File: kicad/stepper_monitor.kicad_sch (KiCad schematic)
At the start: 55 parts, among them J1 Conn_01x04_Male, J2 Conn_01x04_Male, J3 Conn_01x02_Male, J4 USB_C_Receptacle_USB2.0, J5 JTAG, M1 Motor-simple_stepper_motor_an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, Q1 UMH3N, Q2 PJA3439, SW1 SW_Push, U1 CP2102N-A01-GQFN28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

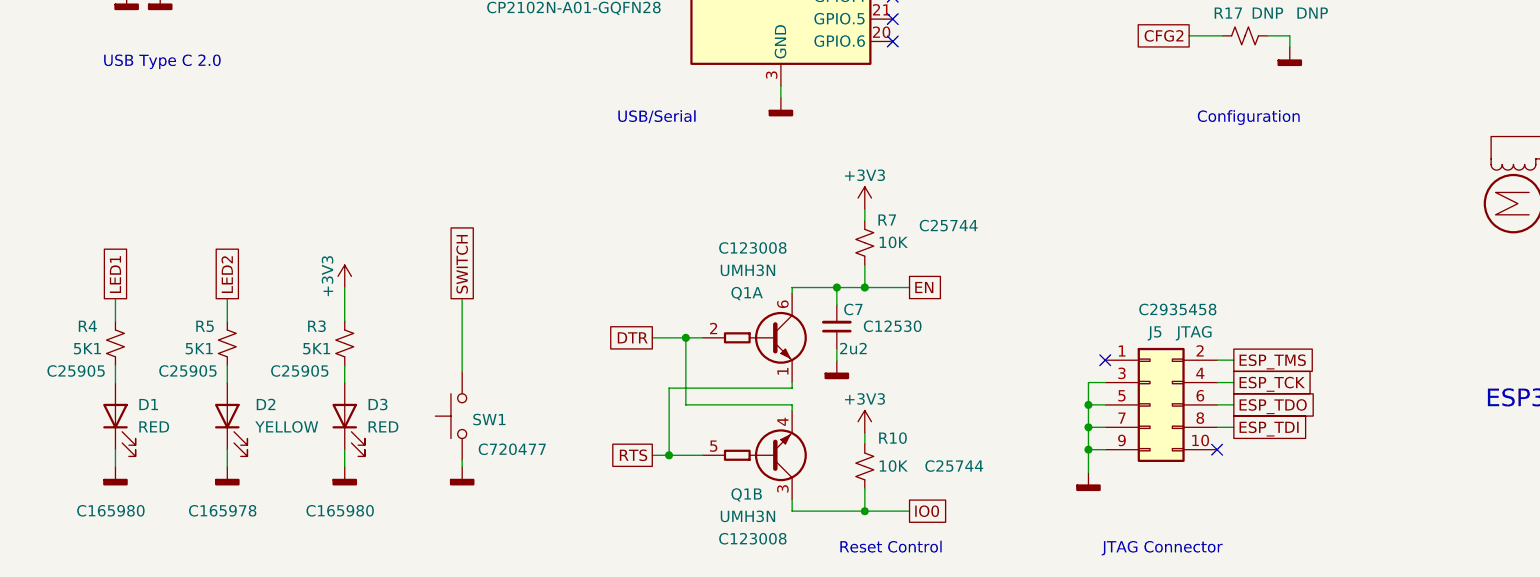
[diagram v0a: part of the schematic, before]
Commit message: Updated led and npn to available parts.
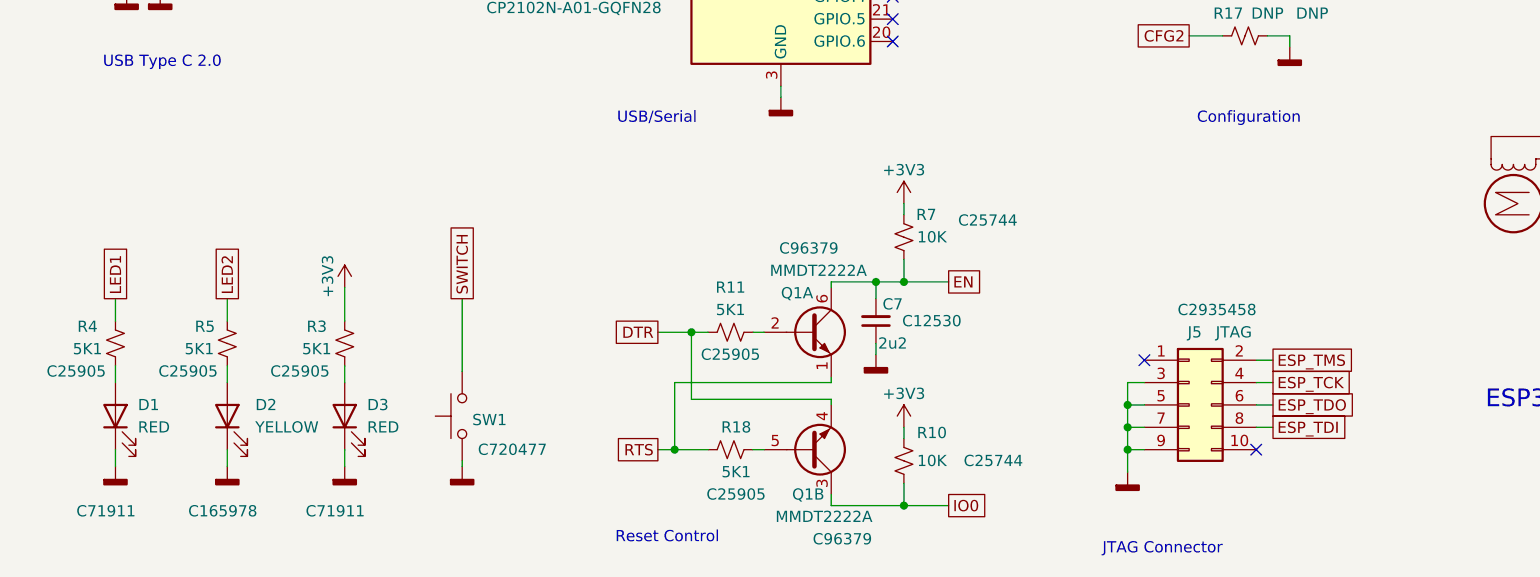
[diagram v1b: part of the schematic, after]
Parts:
- removed Q1: UMH3N, stepper_monitor:SOT-363_SC-70-6, symbol Transistor_BJT:UMH3N
- added Q1: MMDT2222A, stepper_monitor:SOT-363_SC-70-6, symbol Transistor_BJT:MMDT2222A
- added R11, R18: 5K1, Resistor_SMD:R_0402_1005Metric, symbol Device:R_Small_US
- D1, D3: LCSC C165980 -> C71911
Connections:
- net DTR: now also Q1.4 (E2), R11.1
- net EN: now also Q1.6 (C1)
- net IO0: now also Q1.3 (C2)
- net RTS: now also Q1.1 (E1), R18.2
- new net: Q1.2 (B1), R11.2
- new net: Q1.5 (B2), R18.1
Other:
- moved on the sheet: C7, J5, R10, R7

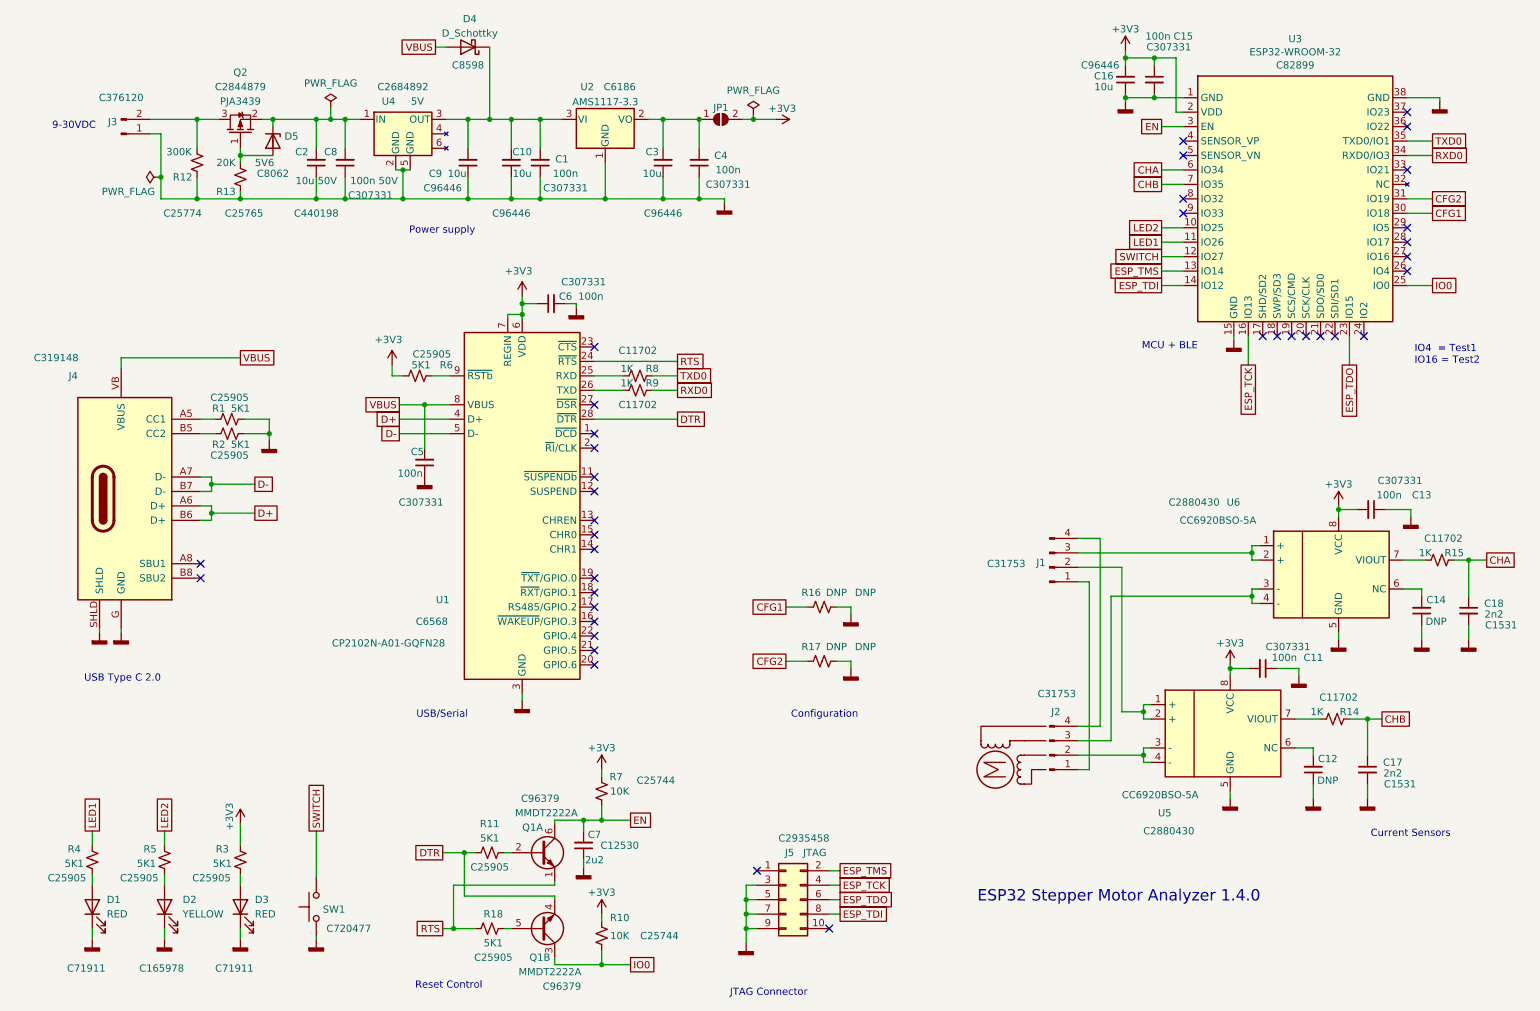
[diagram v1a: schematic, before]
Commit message: Updated PCB for external antenna + cleanups.
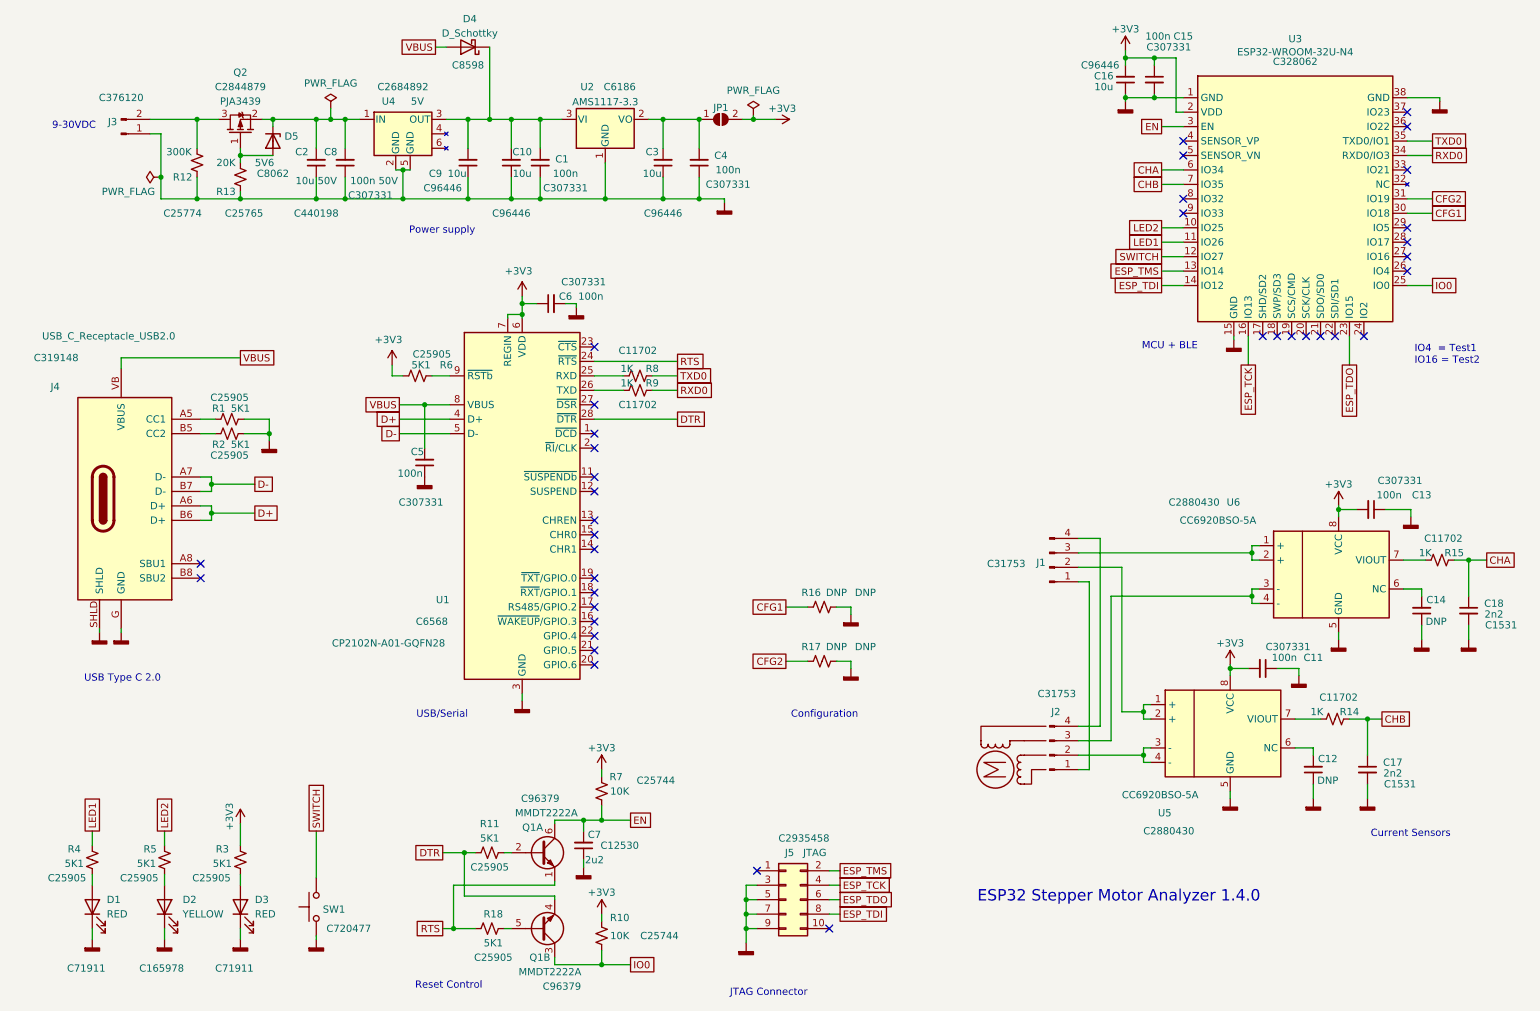
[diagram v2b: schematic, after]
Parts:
- D1, D2, D3: footprint stepper_probe:LED_0402_1005Metric_Pad0.77x0.64mm_HandSolder -> stepper_monitor:LED_0402_1005Metric_Pad0.77x0.64mm_HandSolder
- D5: footprint stepper_monitor:D_MiniMELF_zenner -> Diode_THT:D_DO-41_SOD81_P10.16mm_Horizontal
- J1, J2: footprint stepper_probe:connector_4pins_horizontal -> stepper_monitor:connector_4pins_horizontal
- J3: footprint stepper_probe:PinHeader_1x02_P2.54mm_Horizontal_JLCPCB -> stepper_monitor:PinHeader_1x02_P2.54mm_Horizontal_JLCPCB
- Q1: footprint stepper_monitor:SOT-363_SC-70-6 -> Package_TO_SOT_SMD:SOT-363_SC-70-6
- Q2: footprint stepper_monitor:SOT-23 -> Package_TO_SOT_SMD:SOT-23
- SW1: footprint stepper_probe:SW_Push_SPST_NO_Alps_SKRK -> stepper_monitor:SW_Push_SPST_NO_Alps_SKRK
- U1: footprint stepper_monitor:QFN-28-1EP_5x5mm_P0.5mm_EP3.35x3.35mm -> Package_DFN_QFN:QFN-28-1EP_5x5mm_P0.5mm_EP3.35x3.35mm; symbol stepper_monitor-rescue:CP2102N-A01-GQFN28-Interface_USB -> stepper_monitor:CP2102N-A01-GQFN28-Interface_USB
- U2: footprint stepper_monitor:SOT-223-3_TabPin2 -> Package_TO_SOT_SMD:SOT-223-3_TabPin2
- U3: value ESP32-WROOM-32 -> ESP32-WROOM-32U-N4; footprint stepper_monitor:ESP32-WROOM-32 -> stepper_monitor:ESP32-WROOM-32U; LCSC C82899 -> C328062
- U4: symbol stepper_probe:DC_DC -> stepper_monitor:DC_DC
- U5, U6: footprint stepper_monitor:SOIC-8_3.9x4.9mm_P1.27mm -> Package_SO:SOIC-8_3.9x4.9mm_P1.27mm

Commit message: Fixed schematic footprints.
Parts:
- C12, C14: LCSC (none) -> DNP
- D5: footprint Diode_THT:D_DO-41_SOD81_P10.16mm_Horizontal -> stepper_monitor:D_MiniMELF_zenner
- Q1: footprint Package_TO_SOT_SMD:SOT-363_SC-70-6 -> stepper_monitor:SOT-363_SC-70-6
- Q2: footprint Package_TO_SOT_SMD:SOT-23 -> stepper_monitor:SOT-23
- U1: footprint Package_DFN_QFN:QFN-28-1EP_5x5mm_P0.5mm_EP3.35x3.35mm -> stepper_monitor:QFN-28-1EP_5x5mm_P0.5mm_EP3.35x3.35mm
- U2: footprint Package_TO_SOT_SMD:SOT-223-3_TabPin2 -> stepper_monitor:SOT-223-3_TabPin2
- U5, U6: footprint Package_SO:SOIC-8_3.9x4.9mm_P1.27mm -> stepper_monitor:SOIC-8_3.9x4.9mm_P1.27mm
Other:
- note added: "OK to swap J1, J2 cables."
- note added: "To Stepper Driver"
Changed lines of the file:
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@@
+    (effects (font (size 1.27 1.27)) (justify left bottom))
+  )
+  (text "To Stepper\nDriver" (at 182.88 116.84 0)
     (effects (font (size 1.27 1.27)) (justify left bottom))
   )
@@
   (text "USB/Serial" (at 93.98 142.875 180)
     (effects (font (size 1.27 1.27)) (justify right bottom))
+  )
+  (text "OK to swap \nJ1, J2 cables." (at 182.245 130.81 0)
+    (effects (font (size 1.27 1.27)) (justify left bottom))
   )
   (text "Reset Control" (at 96.52 190.5 180)
@@
     (property "Reference" "U1" (id 0) (at 89.535 121.92 0))
     (property "Value" "CP2102N-A01-GQFN28" (id 1) (at 80.01 129.54 0))
-    (property "Footprint" "Package_DFN_QFN:QFN-28-1EP_5x5mm_P0.5mm_EP3.35x3.35mm" (id 2) (at 114.935 135.89 0)
+    (property "Footprint" "stepper_monitor:QFN-28-1EP_5x5mm_P0.5mm_EP3.35x3.35mm" (id 2) (at 114.935 135.89 0)
       (effects (font (size 1.27 1.27)) (justify left) hide)
     )
@@
     (property "Reference" "U2" (id 0) (at 114.935 31.75 0))
     (property "Value" "AMS1117-3.3" (id 1) (at 118.11 34.3971 0))
-    (property "Footprint" "Package_TO_SOT_SMD:SOT-223-3_TabPin2" (id 2) (at 118.11 32.385 0)
+    (property "Footprint" "stepper_monitor:SOT-223-3_TabPin2" (id 2) (at 118.11 32.385 0)
       (effects (font (size 1.27 1.27)) hide)
     )
@@
       (effects (font (size 1.27 1.27)) hide)
     )
+    (property "LCSC" "DNP" (id 4) (at 245.11 155.575 0))
     (pin "1")
     (pin "2")
@@
       (effects (font (size 1.27 1.27)) (justify left))
     )
-    (property "Footprint" "Package_TO_SOT_SMD:SOT-363_SC-70-6" (id 2) (at 111.76 163.83 0)
+    (property "Footprint" "stepper_monitor:SOT-363_SC-70-6" (id 2) (at 111.76 163.83 0)
       (effects (font (size 1.27 1.27)) hide)
     )
@@
     (property "Reference" "Q2" (id 0) (at 53.975 29.21 90))
     (property "Value" "PJA3439" (id 1) (at 53.975 34.29 90))
-    (property "Footprint" "Package_TO_SOT_SMD:SOT-23" (id 2) (at 55.88 34.925 0)
+    (property "Footprint" "stepper_monitor:SOT-23" (id 2) (at 55.88 34.925 0)
       (effects (font (size 1.27 1.27) italic) (justify left) hide)
     )
@@
       (effects (font (size 1.27 1.27)) (justify left))
     )
-    (property "Footprint" "Package_SO:SOIC-8_3.9x4.9mm_P1.27mm" (id 2) (at 239.395 146.685 0)
+    (property "Footprint" "stepper_monitor:SOIC-8_3.9x4.9mm_P1.27mm" (id 2) (at 239.395 146.685 0)
       (effects (font (size 1.27 1.27) italic) (justify left) hide)
     )
@@
       (effects (font (size 1.27 1.27)) hide)
     )
+    (property "LCSC" "DNP" (id 4) (at 264.16 127.635 0))
     (pin "1")
     (pin "2")
@@
       (effects (font (size 1.27 1.27)) (justify left))
     )
-    (property "Footprint" "Package_TO_SOT_SMD:SOT-363_SC-70-6" (id 2) (at 111.76 182.245 0)
+    (property "Footprint" "stepper_monitor:SOT-363_SC-70-6" (id 2) (at 111.76 182.245 0)
       (effects (font (size 1.27 1.27)) hide)
     )
@@
       (effects (font (size 1.27 1.27)) (justify left))
     )
-    (property "Footprint" "Diode_THT:D_DO-41_SOD81_P10.16mm_Horizontal" (id 2) (at 55.245 41.275 0)
+    (property "Footprint" "stepper_monitor:D_MiniMELF_zenner" (id 2) (at 55.245 41.275 0)
       (effects (font (size 1.27 1.27)) hide)
     )
@@
       (effects (font (size 1.27 1.27)) (justify left))
     )
-    (property "Footprint" "Package_SO:SOIC-8_3.9x4.9mm_P1.27mm" (id 2) (at 258.445 118.745 0)
+    (property "Footprint" "stepper_monitor:SOIC-8_3.9x4.9mm_P1.27mm" (id 2) (at 258.445 118.745 0)
       (effects (font (size 1.27 1.27) italic) (justify left) hide)
     )
@@
   (symbol (lib_id "Connector:Conn_01x04_Male") (at 196.215 116.205 0) (mirror x) (unit 1)
     (in_bom yes) (on_board yes)
-    (property "Reference" "J1" (id 0) (at 195.5038 115.3688 0)
+    (property "Reference" "J1" (id 0) (at 198.12 108.585 0)
       (effects (font (size 1.27 1.27)) (justify right))
     )
@@
       (effects (font (size 1.27 1.27)) hide)
     )
-    (property "LCSC" "C31753" (id 4) (at 188.595 115.57 0))
+    (property "LCSC" "C31753" (id 4) (at 197.485 105.41 0))
     (pin "1")
     (pin "2")
@@
     )
     (path "/c7db2209-f5b4-472f-80a6-506d3059107d"
-      (reference "D5") (unit 1) (value "5V6") (footprint "Diode_THT:D_DO-41_SOD81_P10.16mm_Horizontal")
+      (reference "D5") (unit 1) (value "5V6") (footprint "stepper_monitor:D_MiniMELF_zenner")
     )
     (path "/eeca56e9-7b7a-4092-8038-da05fc334f53"
@@
     )
     (path "/3832b426-1a57-444e-8080-6308dd8dcb96"
-      (reference "Q1") (unit 1) (value "MMDT2222A") (footprint "Package_TO_SOT_SMD:SOT-363_SC-70-6")
+      (reference "Q1") (unit 1) (value "MMDT2222A") (footprint "stepper_monitor:SOT-363_SC-70-6")
     )
     (path "/acea237b-900b-468d-8004-c9a98cf25323"
-      (reference "Q1") (unit 2) (value "MMDT2222A") (footprint "Package_TO_SOT_SMD:SOT-363_SC-70-6")
+      (reference "Q1") (unit 2) (value "MMDT2222A") (footprint "stepper_monitor:SOT-363_SC-70-6")
     )
     (path "/420a49fa-bc07-40b0-8b18-684ba9455b7a"
-      (reference "Q2") (unit 1) (value "PJA3439") (footprint "Package_TO_SOT_SMD:SOT-23")
+      (reference "Q2") (unit 1) (value "PJA3439") (footprint "stepper_monitor:SOT-23")
     )
     (path "/00000000-0000-0000-0000-000063145bc1"
@@
     )
     (path "/00000000-0000-0000-0000-0000631b04ca"
-      (reference "U1") (unit 1) (value "CP2102N-A01-GQFN28") (footprint "Package_DFN_QFN:QFN-28-1EP_5x5mm_P0.5mm_EP3.35x3.35mm")
+      (reference "U1") (unit 1) (value "CP2102N-A01-GQFN28") (footprint "stepper_monitor:QFN-28-1EP_5x5mm_P0.5mm_EP3.35x3.35mm")
     )
     (path "/170ecade-8817-49a1-92ea-e91fd90a65e6"
-      (reference "U2") (unit 1) (value "AMS1117-3.3") (footprint "Package_TO_SOT_SMD:SOT-223-3_TabPin2")
+      (reference "U2") (unit 1) (value "AMS1117-3.3") (footprint "stepper_monitor:SOT-223-3_TabPin2")
     )
     (path "/00000000-0000-0000-0000-00006319c305"
@@
     )
     (path "/8e00d3f2-b2b5-4f8f-bf38-86ce986b1bcf"
-      (reference "U5") (unit 1) (value "CC6920BSO-5A") (footprint "Package_SO:SOIC-8_3.9x4.9mm_P1.27mm")
+      (reference "U5") (unit 1) (value "CC6920BSO-5A") (footprint "stepper_monitor:SOIC-8_3.9x4.9mm_P1.27mm")
     )
     (path "/cb5ee068-cc95-4818-84e7-6b246cf90ff1"
-      (reference "U6") (unit 1) (value "CC6920BSO-5A") (footprint "Package_SO:SOIC-8_3.9x4.9mm_P1.27mm")
-    )
-  )
+      (reference "U6") (unit 1) (value "CC6920BSO-5A") (footprint "stepper_monitor:SOIC-8_3.9x4.9mm_P1.27mm")
+    )
+  )
